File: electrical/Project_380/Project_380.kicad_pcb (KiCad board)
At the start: 2 copper layers, 80.9 x 50 mm, 34 parts, among them J1 FL_Motor, J10 ToF 2, J11 ToF 3, J12 ToF 4, J13 IMU, J14 UART_to_USB, J15 DWN_Motor, J16 Switch, J2 RL_Motor, J3 FR_Motor, J4 RR_Motor, J5 Battery, J6 Battery, J7 Battery, J8 Battery, J9 ToF 1, SW1 SW_SPST, U1 HW613, U2 ESP32-WROOM, U3 NX3L4051PW,118, U4 , U5 , U6 NX3L4051PW,118

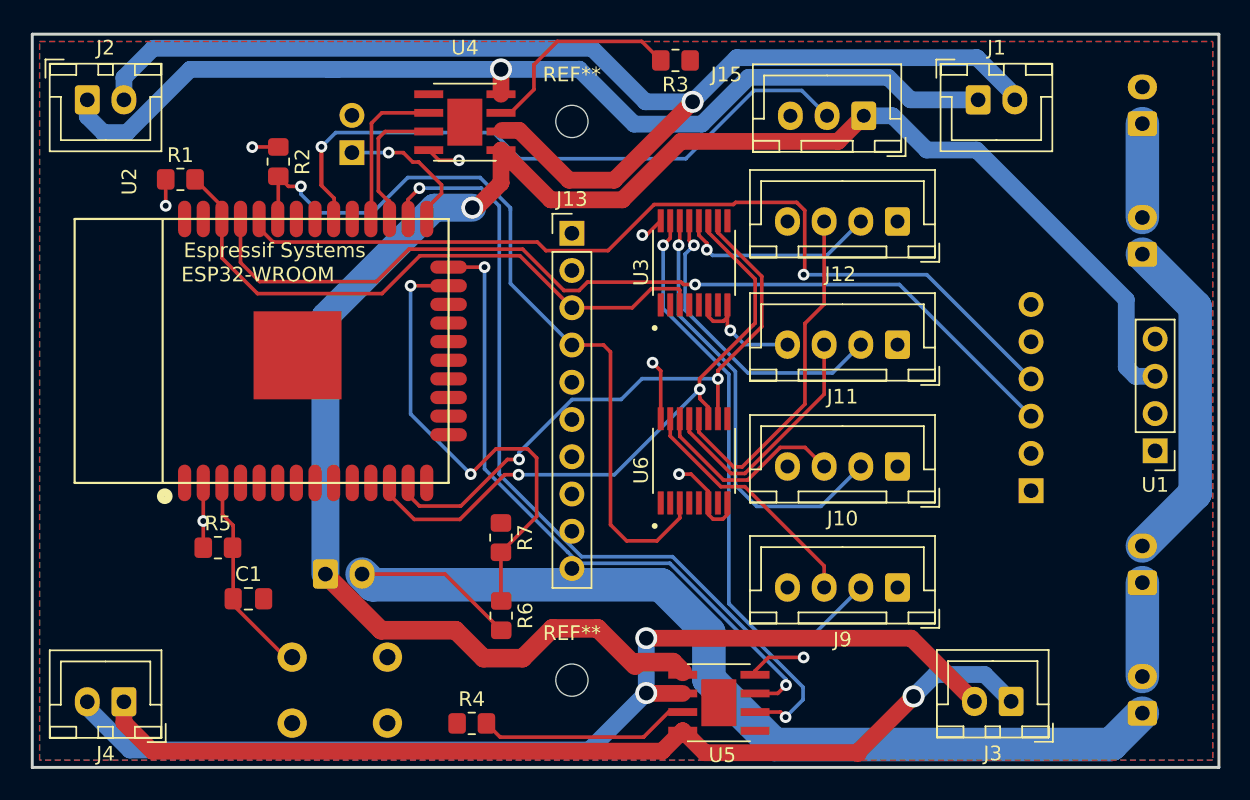
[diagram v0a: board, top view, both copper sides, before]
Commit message: Make fixes to board, add silkscreen, and generate gerbers
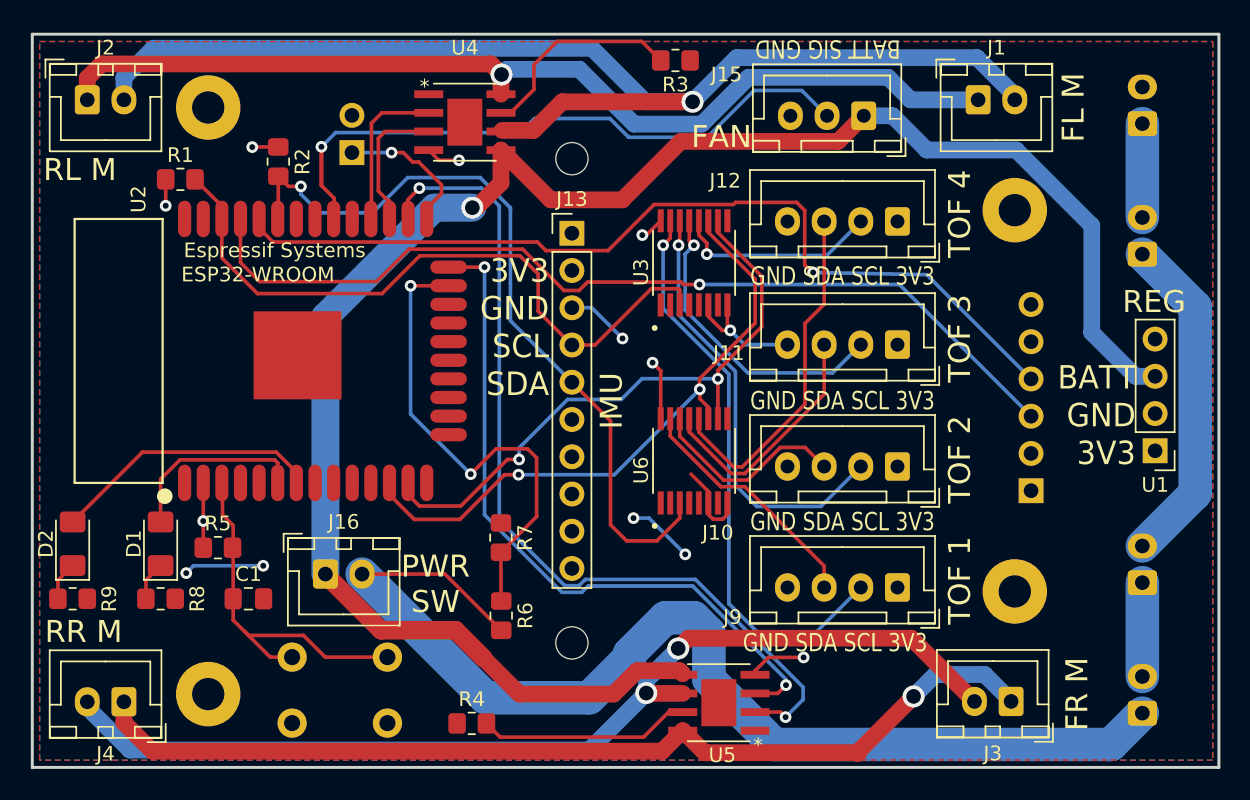
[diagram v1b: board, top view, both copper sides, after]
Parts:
- added D1: LED, LED_SMD:LED_1206_3216Metric_Pad1.42x1.75mm_HandSolder, F.Cu at (108.8, 94.8)
- added D2: LED, LED_SMD:LED_1206_3216Metric_Pad1.42x1.75mm_HandSolder, F.Cu at (102.8, 94.8)
- added G***: LOGO, Main project:emu, B.Cu at (116.5, 89.0)
- added R8: 120, Resistor_SMD:R_0805_2012Metric_Pad1.20x1.40mm_HandSolder, F.Cu at (108.8, 98.5)
- added R9: 120, Resistor_SMD:R_0805_2012Metric_Pad1.20x1.40mm_HandSolder, F.Cu at (102.8, 98.5)
- added REF**: MountingHole_2.2mm_M2_Pad, MountingHole:MountingHole_2.2mm_M2_Pad, F.Cu at (112.0, 65.0)
- added REF**: MountingHole_2.2mm_M2_Pad, MountingHole:MountingHole_2.2mm_M2_Pad, F.Cu at (167.0, 98.0)
- added REF**: MountingHole_2.2mm_M2_Pad, MountingHole:MountingHole_2.2mm_M2_Pad, F.Cu at (112.0, 105.0)
- added REF**: MountingHole_2.2mm_M2_Pad, MountingHole:MountingHole_2.2mm_M2_Pad, F.Cu at (167.0, 72.0)
- J16: moved to F.Cu
- U4, U5: value (none) -> TB67H451FNG_EL
- moved REF** 2.54 mm to (136.8, 101.5)
- moved REF** 2.54 mm to (136.8, 68.5)
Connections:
- J13 pad 3: /Sensors/SCL -> GND
- J13 pad 4: /Sensors/SDA -> /Sensors/SCL
- J13 pad 5: GND -> /Sensors/SDA
- U2 pad 6: unconnected-(U2-Pad6) -> Net-(U2-Pad6)
- U2 pad 7: unconnected-(U2-Pad7) -> Net-(U2-Pad7)
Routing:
- net Net-(U2-Pad7): track 0.00 -> 18.5 mm
- net GND: track 15.7 -> 28.7 mm, vias 2 -> 6
- net Net-(U2-Pad6): track 0.00 -> 12.9 mm
- net Net-(C1-Pad1): track 14.3 -> 25.2 mm
- net Net-(J16-Pad2): track 71.8 -> 76.5 mm
- net /Sensors/SCL: track 42.6 -> 46.1 mm
- net Net-(J1-Pad2): track 84.2 -> 81.0 mm
- net Net-(D2-Pad1): track 0.00 -> 2.68 mm
- net Net-(D1-Pad1): track 0.00 -> 2.68 mm
- net /Motor Control/M_CTL_R2: track 58.2 -> 60.3 mm
- net Net-(J1-Pad1): track 70.0 -> 67.9 mm
- net /Motor Control/M_CTL_R1: track 45.5 -> 47.3 mm
- net Net-(J3-Pad2): track 71.7 -> 70.0 mm
- net +BATT: track 122.7 -> 124.1 mm
- net /Sensors/SDA: track 54.5 -> 53.2 mm
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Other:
- board text added: "- +"
- board text added: "3V3 GND SCL SDA"
- board text added: "BATT GND 3V3"
- board text added: "BATT SIG GND"
- board text added: "Batteries"
- board text added: "E.M.U. WRANGLER"
- board text added: "FAN"
- board text added: "FL M"
- board text added: "FR M"
- board text added: "GND SDA SCL 3V3"
- board text added: "IMU"
- board text added: "K. K. Ray & Z. Mears 2022-03-01"
- board text added: "NC(5V) GND RXD TXD NC 3V3"
- board text added: "PWR SW"
- board text added: "Programming"
- board text added: "REG"
- board text added: "RESET"
- board text added: "RL M"
- board text added: "RR M"
- board text added: "TOF 1"
- board text added: "TOF 2"
- board text added: "TOF 3"
- board text added: "TOF 4"
- board text added: "prog jmpr"
